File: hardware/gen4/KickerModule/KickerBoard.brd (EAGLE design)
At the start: 328.9 x 149.3 mm, 119 parts

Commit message: moving things around
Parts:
- moved U$8 16.2 mm to (6.35, 90.8)
- moved U$9 14.2 mm to (138.4, 89.5)
- moved JP2 6.02 mm to (136.5, 96.5), flipped to the top, turned to 90 degrees
- moved KICK_Q 2.29 mm to (125.1, 113.7)
- moved MOTOR2 1.27 mm to (56.5, 66.0)
- moved C14 0.63 mm to (88.0, 135.8)
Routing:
- net GND: track 755.3 -> 630.7 mm, vias 29 -> 28
- net N$38: track 93.9 -> 6.08 mm, vias 1 -> 0
- net 12VGND: track 684.0 -> 653.0 mm
- net N$43: track 61.5 -> 36.1 mm
- net N$44: track 68.7 -> 44.9 mm
- net N$39: track 69.8 -> 46.2 mm, vias 1 -> 0
- net MISO: track 231.0 -> 208.1 mm
- net N$45: track 73.1 -> 50.9 mm
- net N$37: track 93.8 -> 71.8 mm
- net MOSI: track 209.8 -> 189.4 mm
- net SCK: track 215.3 -> 195.2 mm, vias 8 -> 7
- net N$56: track 65.8 -> 49.6 mm
- net N$55: track 63.6 -> 48.0 mm
- net N$42: track 52.7 -> 37.2 mm
- net N$54: track 61.1 -> 46.0 mm
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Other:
- board size 328.9 x 149.3 mm -> 320.2 x 149.3 mm

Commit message: routing in progress
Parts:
- moved JP4 24.4 mm to (0.64, 56.5), flipped to the top, turned to 270 degrees
- moved U$8 19.7 mm to (1.27, 71.8)
- moved JP3 15.5 mm to (137.2, 48.3)
- moved U$10 15.4 mm to (137.8, 63.5)
- moved R25 15.1 mm to (31.1, 130.5), flipped to the bottom, turned to 180 degrees
- moved U$6 15.1 mm to (27.9, 139.1), turned to 270 degrees
- moved DRIB_TRAN 13.7 mm to (24.1, 34.3), turned to 180 degrees
- moved GND_TEST 11.4 mm to (30.5, 12.7), flipped to the top
- moved R16 9.21 mm to (31.1, 133.7), flipped to the bottom
- moved R3 8.98 mm to (31.1, 132.1), flipped to the bottom
- moved JP2 8.64 mm to (139.1, 88.3)
- moved MOTOR1 8.54 mm to (15.9, 67.9)
- moved JP1 8.28 mm to (0.64, 67.9)
- moved R13 8.13 mm to (31.1, 137.2), flipped to the bottom
- moved R22 7.96 mm to (39.4, 19.1)
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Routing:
- net 3.3V: track 496.4 -> 225.3 mm, vias 15 -> 6
- net GND: track 630.7 -> 426.5 mm, vias 28 -> 21
- net 12VGND: track 653.0 -> 459.4 mm, vias 13 -> 5
- net MISO: track 208.1 -> 59.1 mm, vias 11 -> 3
- net SCK: track 195.2 -> 60.1 mm, vias 7 -> 3
- net MOSI: track 189.4 -> 73.6 mm, vias 9 -> 5
- net M1QB-4: track 91.5 -> 0.00 mm, vias 5 -> 0
- net SS4: track 130.3 -> 39.9 mm
- net N$38: track 6.08 -> 90.4 mm, vias 0 -> 1
- net N$43: track 36.1 -> 102.5 mm
- net N$42: track 37.2 -> 98.7 mm
- net N$44: track 44.9 -> 104.2 mm
- net N$45: track 50.9 -> 107.8 mm
- net M1QA-2: track 55.4 -> 0.00 mm, vias 3 -> 0
- net N$39: track 46.2 -> 101.0 mm, vias 0 -> 1
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
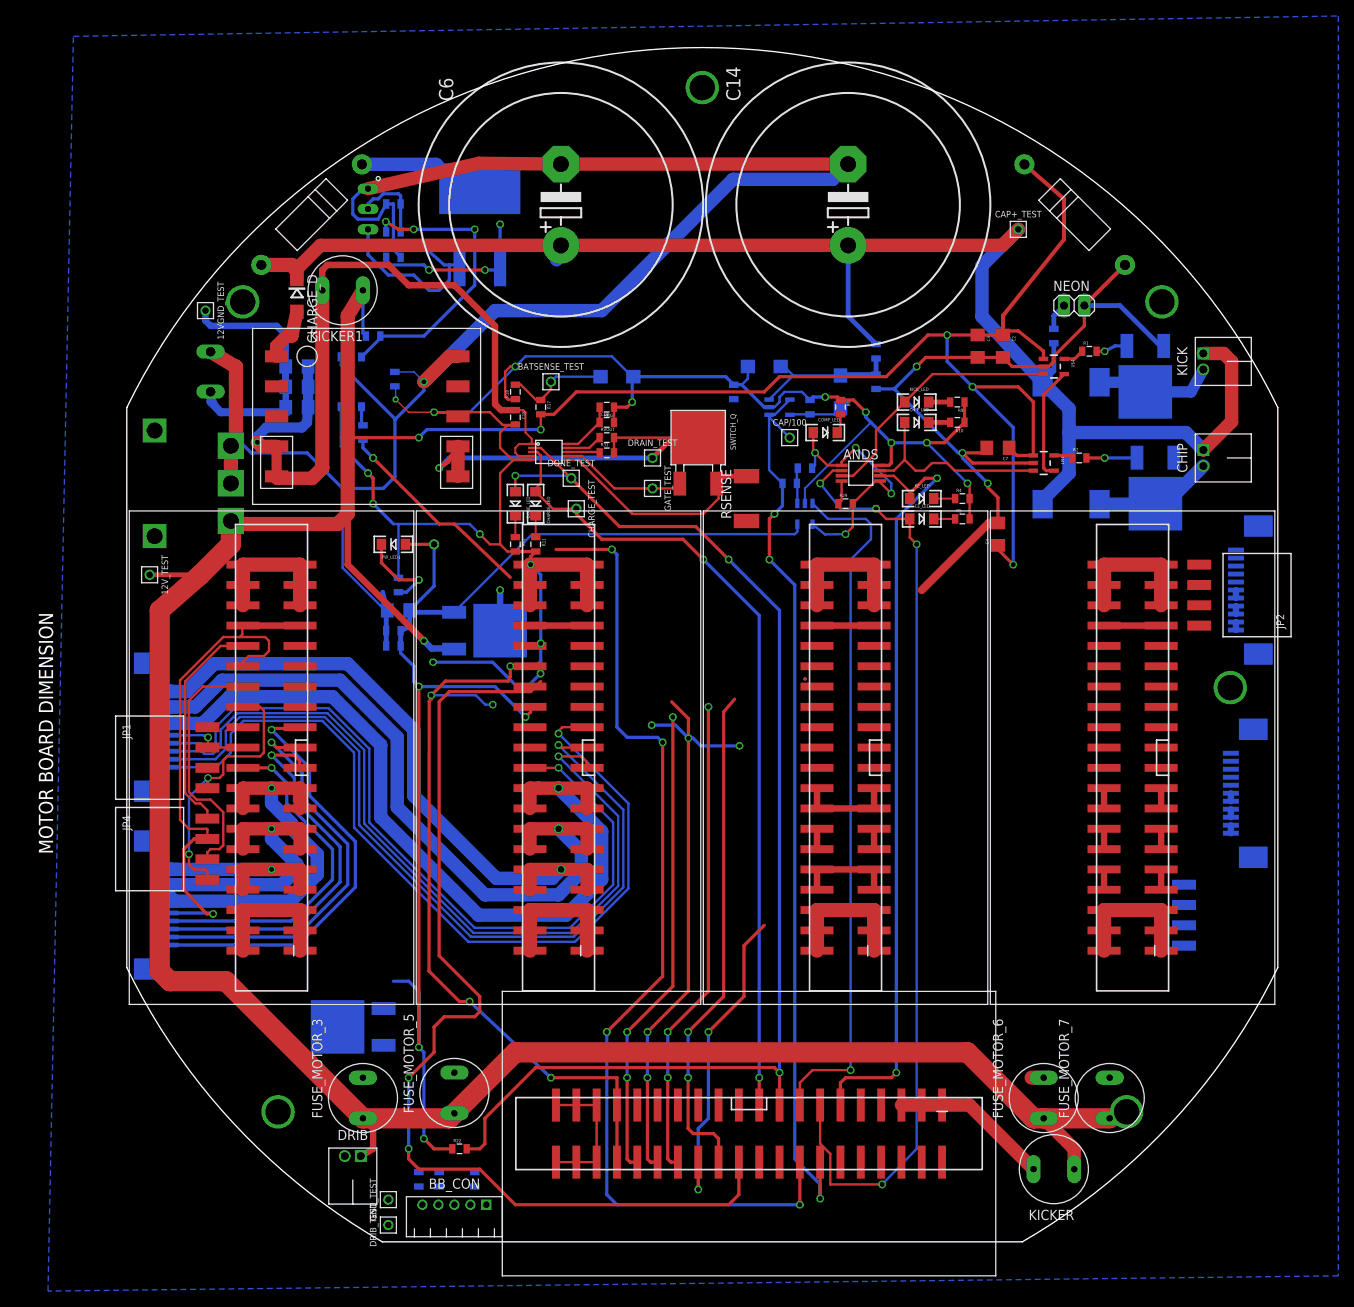
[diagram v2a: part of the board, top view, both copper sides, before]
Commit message: almost done routing v2
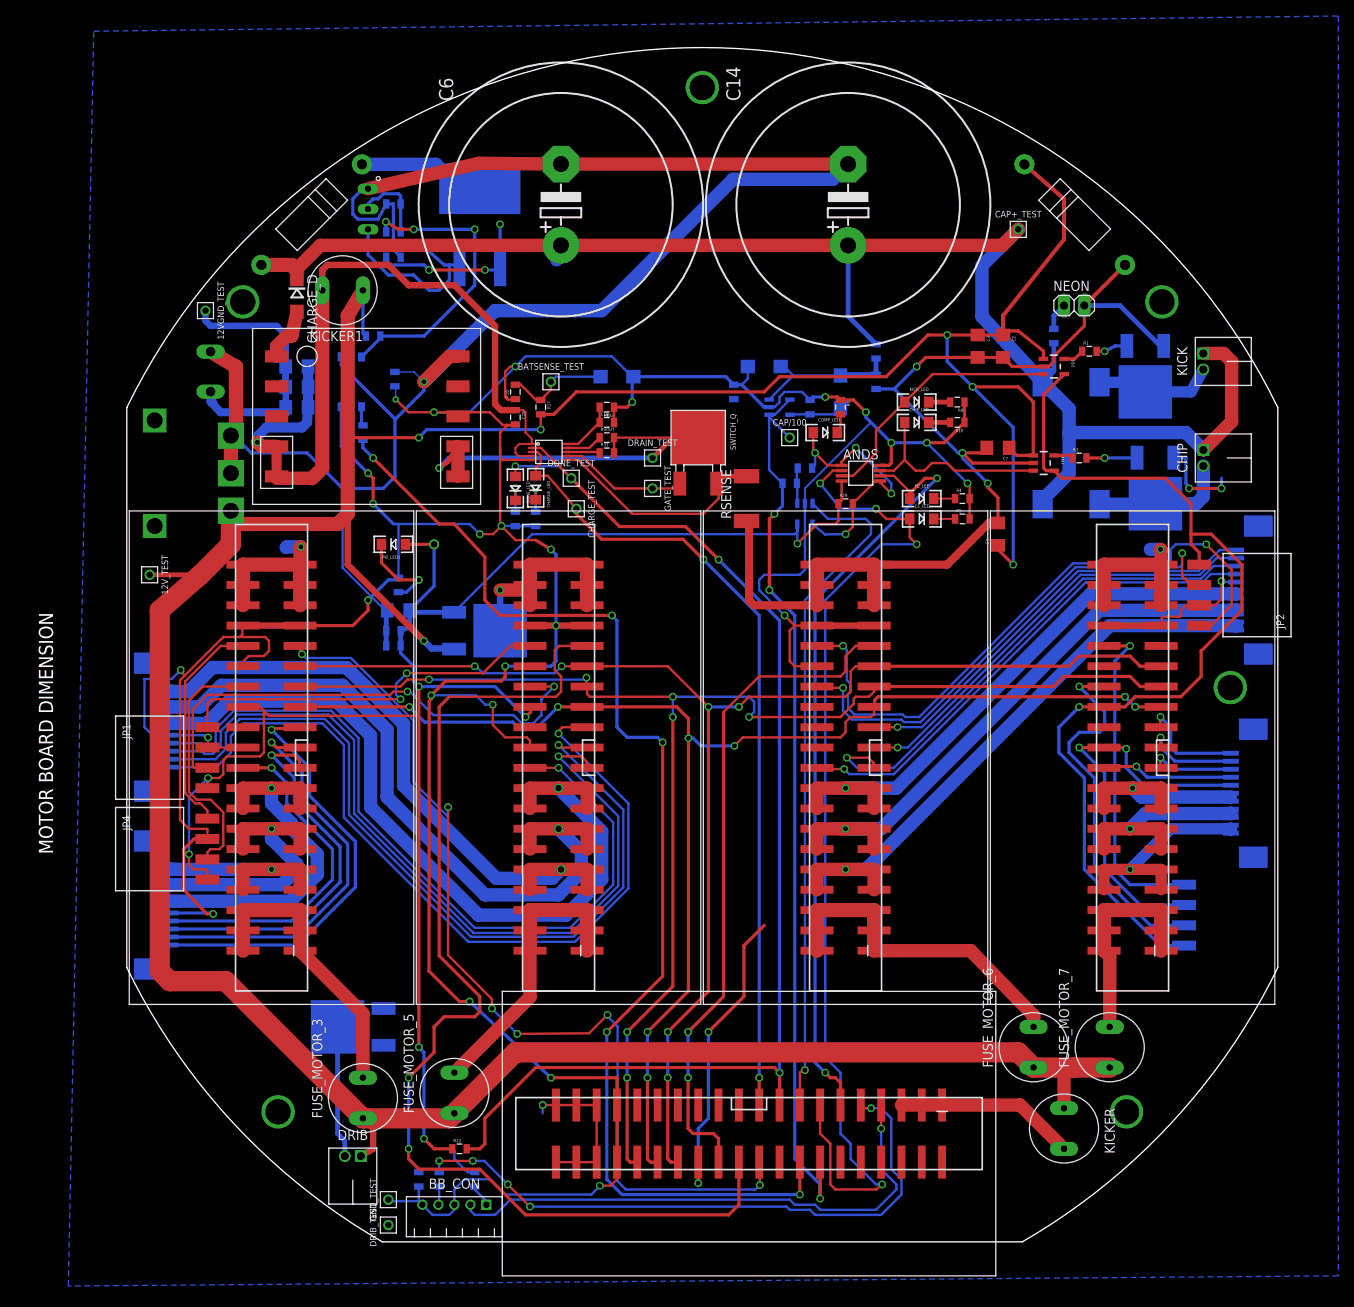
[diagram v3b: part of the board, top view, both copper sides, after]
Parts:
- moved FUSE_MOTOR_6 6.48 mm to (111.1, 31.8)
- moved FUSE_MOTOR_7 6.35 mm to (120.7, 31.8)
- moved KICKER 5.24 mm to (114.9, 21.6), turned to 270 degrees
- moved R11 3.18 mm to (48.9, 97.8), flipped to the bottom
- moved R12 3.18 mm to (46.4, 97.8), flipped to the bottom
- moved CHARGE_LED 1.98 mm to (48.9, 101.7)
- moved DONE_LED 1.91 mm to (46.4, 101.6)
- moved ON/OFF 1.27 mm to (10.8, 103.5)
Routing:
- net GND: track 426.5 -> 610.0 mm, vias 21 -> 29
- net 3.3V: track 225.3 -> 360.7 mm, vias 6 -> 8
- net SS1: track 0.00 -> 120.3 mm, vias 0 -> 6
- net MISO: track 59.1 -> 178.3 mm, vias 3 -> 7
- net SCK: track 60.1 -> 175.2 mm, vias 3 -> 6
- net MOSI: track 73.6 -> 174.4 mm, vias 5 -> 8
- net M1QB-3: track 0.00 -> 80.5 mm, vias 0 -> 2
- net BB_OUT: track 0.00 -> 77.6 mm, vias 0 -> 5
- net BB_IN: track 0.00 -> 67.9 mm, vias 0 -> 1
- net N$55: track 6.08 -> 73.9 mm, vias 0 -> 1
- net M1QA-3: track 0.00 -> 64.2 mm, vias 0 -> 2
- net N$59: track 0.00 -> 63.9 mm, vias 0 -> 1
- net N$58: track 0.00 -> 63.1 mm, vias 0 -> 1
- net M1QA-2: track 0.00 -> 62.8 mm, vias 0 -> 2
- net N$54: track 13.2 -> 75.3 mm, vias 0 -> 1
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
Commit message: mainboard done w errors
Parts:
- moved 12V_TEST 1.42 mm to (1.27, 92.1)
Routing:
- net 3.3V: track 360.7 -> 490.8 mm, vias 8 -> 13
- net SS4: track 38.3 -> 133.0 mm, vias 2 -> 4
- net DRIB: track 0.00 -> 85.5 mm, vias 0 -> 3
- net GND: track 610.0 -> 680.9 mm, vias 29 -> 33
- net N$18: track 9.84 -> 20.2 mm, vias 0 -> 1
- net 12VGND: track 509.9 -> 513.0 mm
- net N$68: track 12.0 -> 14.7 mm
- net DIVCAP: track 113.9 -> 114.9 mm
- net M1QB-1: track 27.7 -> 28.6 mm
- net 12V: track 461.1 -> 460.3 mm
- net M1QA-2: track 62.8 -> 63.4 mm
- net M1QA-1: track 31.6 -> 32.2 mm

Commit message: new mouting hole
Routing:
- net CAP+: track 195.6 -> 193.7 mm
- net 12V: track 460.3 -> 458.5 mm
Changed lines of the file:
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@@
 <wire x1="87.95" y1="123.135" x2="91.44" y2="119.645" width="0.6096" layer="16"/>
 <wire x1="52.05" y1="131.985" x2="51.975" y2="131.985" width="1.6764" layer="1"/>
-<wire x1="51.975" y1="131.985" x2="51.435" y2="131.445" width="1.6764" layer="1"/>
 <wire x1="51.435" y1="131.445" x2="51.514375" y2="131.445" width="1.6764" layer="1"/>
 <wire x1="51.514375" y1="131.445" x2="51.101875" y2="131.0325" width="1.6764" layer="1"/>
 <wire x1="51.101875" y1="131.0325" x2="21.429375" y2="131.0325" width="1.6764" layer="1"/>
-<wire x1="51.51" y1="130.175" x2="52.05" y2="131.985" width="1.6764" layer="16"/>
 <contactref element="U$7" pad="+"/>
 <wire x1="14.605" y1="129.54" x2="18.415" y2="129.54" width="1.778" layer="1"/>
@@
 <wire x1="18.905" y1="128.905" x2="19.05" y2="129.05" width="1.6764" layer="1"/>
 <wire x1="19.05" y1="129.05" x2="21.429375" y2="131.0325" width="1.6764" layer="1"/>
+<wire x1="51.514375" y1="131.445" x2="51.514375" y2="131.449375" width="0.4064" layer="1"/>
+<wire x1="51.514375" y1="131.449375" x2="52.05" y2="131.985" width="0.4064" layer="1"/>
 </signal>
 <signal name="CHIP_ENABLE">
@@
 <wire x1="10.795" y1="98.806" x2="10.795" y2="95.885" width="2.54" layer="1"/>
 <wire x1="10.795" y1="95.885" x2="6.985" y2="92.075" width="2.54" layer="1"/>
-<wire x1="6.985" y1="92.075" x2="1.27" y2="92.075" width="0.6096" layer="1"/>
 <wire x1="10.795" y1="98.806" x2="11.049" y2="97.155" width="0.6096" layer="1"/>
 <wire x1="3.175" y1="40.005" x2="10.16" y2="40.005" width="2.54" layer="1"/>
@@
 <wire x1="27.675" y1="120.65" x2="27.305" y2="121.02" width="0.4064" layer="16"/>
 <wire x1="27.305" y1="121.02" x2="27.305" y2="126.365" width="0.4064" layer="16"/>
-<wire x1="6.985" y1="92.075" x2="1.905" y2="86.995" width="2.54" layer="1"/>
-<wire x1="1.905" y1="86.995" x2="1.905" y2="41.275" width="2.54" layer="1"/>
-<wire x1="1.905" y1="41.275" x2="3.175" y2="40.005" width="2.54" layer="1"/>
+<wire x1="6.985" y1="92.075" x2="1.27" y2="92.075" width="2.54" layer="1"/>
+<wire x1="1.27" y1="92.075" x2="1.27" y2="41.91" width="2.54" layer="1"/>
+<wire x1="1.27" y1="41.91" x2="3.175" y2="40.005" width="2.54" layer="1"/>
 <contactref element="U$12" pad="-"/>
 <wire x1="109.982640625" y1="142.11235625" x2="114.935" y2="137.794996875" width="0.508" layer="1"/>
@@
 <signal name="N$49">
 <via x="135.723884375" y="76.708" extent="1-16" drill="3.175"/>
+<via x="6.183884375" y="87.503" extent="1-16" drill="3.175"/>
+<wire x1="6.183884375" y1="87.503" x2="135.723884375" y2="76.708" width="0" layer="19" extent="1-1"/>
 </signal>
 </signals>

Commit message: few fixes
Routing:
- net N$21: track 20.9 -> 15.4 mm, vias 3 -> 2
- net 12V-KICKER: track 122.9 -> 122.0 mm
- net N$29: vias 3 -> 2

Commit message: Panelizing
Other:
- board size 320.2 x 149.3 mm -> 143.9 x 149.3 mm
- board text added: "C:/Users/JohnAlex/Downloads/1053199_481094518647458_1043735417_o.bmp"

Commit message: more fixes
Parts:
- moved U$11 1.91 mm to (1.08, 51.4)
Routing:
- net N$46: track 26.4 -> 27.9 mm
- net GND: track 680.9 -> 682.4 mm
- net N$48: track 46.6 -> 45.6 mm
- net N$53: track 53.8 -> 53.2 mm
- net M1QB-1: track 28.6 -> 29.3 mm
- net N$52: track 50.4 -> 49.8 mm
- net N$51: track 47.8 -> 47.2 mm
- net N$50: track 43.1 -> 42.5 mm
